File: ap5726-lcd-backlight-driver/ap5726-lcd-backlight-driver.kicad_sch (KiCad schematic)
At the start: 7 parts, among them J1 Conn_01x05_Pin

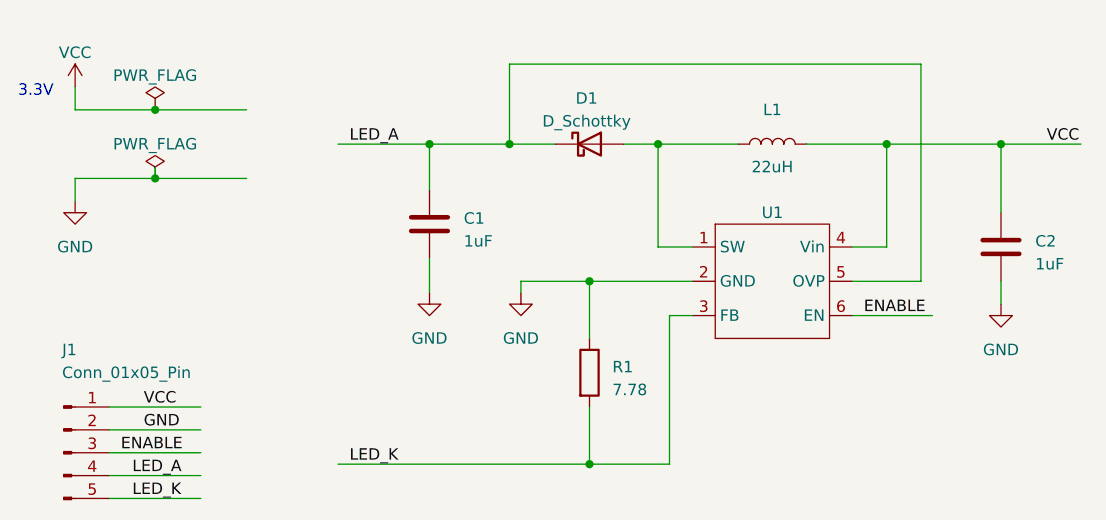
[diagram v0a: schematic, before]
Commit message: Add testpoint and jumper to feedback on AP5726.
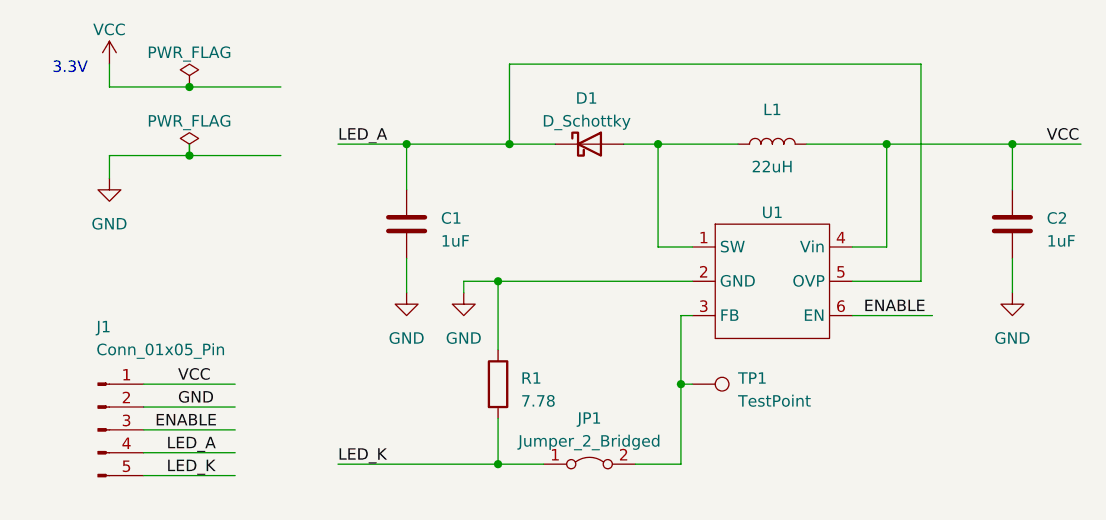
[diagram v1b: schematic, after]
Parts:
- added JP1: Jumper_2_Bridged, symbol Jumper:Jumper_2_Bridged
- added TP1: TestPoint, symbol Connector:TestPoint
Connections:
- net LED_K: now also JP1.1 (A); no longer U1.3 (FB)
- new net: JP1.2 (B), TP1.1, U1.3 (FB)
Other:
- moved on the sheet: C1, C2, J1, R1

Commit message: Add all footprints except inductor.
Import footprint and step model for AP5726 from mouser.
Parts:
- C1, C2: footprint (none) -> Capacitor_SMD:C_0805_2012Metric
- D1: footprint (none) -> Diode_SMD:D_SOD-123
- J1: footprint (none) -> Connector_PinHeader_2.54mm:PinHeader_1x05_P2.54mm_Vertical
- JP1: footprint (none) -> Connector_PinHeader_2.54mm:PinHeader_1x02_P2.54mm_Vertical
- R1: footprint (none) -> Resistor_SMD:R_0805_2012Metric
- TP1: footprint (none) -> TestPoint:TestPoint_THTPad_D2.0mm_Drill1.0mm
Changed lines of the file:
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@@
       (effects (font (size 1.27 1.27)))
     )
-    (property "Footprint" "" (at 158.75 88.9 0)
+    (property "Footprint" "Diode_SMD:D_SOD-123" (at 158.75 88.9 0)
       (effects (font (size 1.27 1.27)) hide)
     )
@@
       (effects (font (size 1.27 1.27)) (justify left))
     )
-    (property "Footprint" "" (at 139.3952 101.6 0)
+    (property "Footprint" "Capacitor_SMD:C_0805_2012Metric" (at 139.3952 101.6 0)
       (effects (font (size 1.27 1.27)) hide)
     )
@@
       (effects (font (size 1.27 1.27)) (justify left))
     )
-    (property "Footprint" "" (at 170.18 120.65 0)
+    (property "Footprint" "TestPoint:TestPoint_THTPad_D2.0mm_Drill1.0mm" (at 170.18 120.65 0)
       (effects (font (size 1.27 1.27)) hide)
     )
@@
       (effects (font (size 1.27 1.27)))
     )
-    (property "Footprint" "" (at 158.75 124.46 0)
+    (property "Footprint" "Connector_PinHeader_2.54mm:PinHeader_1x02_P2.54mm_Vertical" (at 158.75 124.46 0)
       (effects (font (size 1.27 1.27)) hide)
     )
@@
       (effects (font (size 1.27 1.27)) (justify left))
     )
-    (property "Footprint" "" (at 146.812 115.57 90)
+    (property "Footprint" "Resistor_SMD:R_0805_2012Metric" (at 146.812 115.57 90)
       (effects (font (size 1.27 1.27)) hide)
     )
@@
       (effects (font (size 1.27 1.27)) (justify left))
     )
-    (property "Footprint" "" (at 206.7052 101.6 0)
+    (property "Footprint" "Capacitor_SMD:C_0805_2012Metric" (at 206.7052 101.6 0)
       (effects (font (size 1.27 1.27)) hide)
     )
@@
       (effects (font (size 1.27 1.27)))
     )
-    (property "Footprint" "" (at 104.14 120.65 0)
-      (effects (font (size 1.27 1.27)) hide)
-    )
+    (property "Footprint" "Connector_PinHeader_2.54mm:PinHeader_1x05_P2.54mm_Vertical" (at 104.14 120.65 0)
+      (effects (font (size 1.27 1.27)) hide)
+    )

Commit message: Add step model and footprint for Murata inductor.
The step model doesn't include connections between pins and the inductor
coil in the middle, nor does it have the contour of the resin on the
bottom of the part. This is probably good enough, but I will need to get
a physical part if I want to add more detail (they're in the mail).
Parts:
- L1: footprint (none) -> project:lqh44pn220mprl
- U1: footprint (none) -> project:ap5726-sot26
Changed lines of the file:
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@@
       (effects (font (size 1.27 1.27)))
     )
-    (property "Footprint" "" (at 179.07 88.9 0)
+    (property "Footprint" "project:lqh44pn220mprl" (at 179.07 88.9 0)
       (effects (font (size 1.27 1.27)) hide)
     )
@@
       (effects (font (size 1.27 1.27)))
     )
-    (property "Footprint" "" (at 173.99 96.52 0)
+    (property "Footprint" "project:ap5726-sot26" (at 173.99 96.52 0)
       (effects (font (size 1.27 1.27)) hide)
     )

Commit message: Initial PCB layout and footprint fixes for AP5726.
Note to self: maybe we should ask EEVblog forum members for a PCB layout
critique? Could be painful...
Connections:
- net ENABLE: now also U1.4 (EN); no longer U1.6 (EN)
- net VCC: now also U1.6 (Vin); no longer U1.4 (Vin)

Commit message: Redo AP5726 pcb layout using fill zones.
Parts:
- JP1: footprint Connector_PinHeader_2.54mm:PinHeader_1x02_P2.54mm_Vertical -> Jumper:SolderJumper-2_P1.3mm_Bridged_Pad1.0x1.5mm
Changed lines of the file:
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@@
       (effects (font (size 1.27 1.27)))
     )
-    (property "Footprint" "Connector_PinHeader_2.54mm:PinHeader_1x02_P2.54mm_Vertical" (at 158.75 124.46 0)
+    (property "Footprint" "Jumper:SolderJumper-2_P1.3mm_Bridged_Pad1.0x1.5mm" (at 158.75 124.46 0)
       (effects (font (size 1.27 1.27)) hide)
     )
